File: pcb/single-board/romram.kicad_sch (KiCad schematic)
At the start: 26 parts, among them U10 74HC00, U11 74HC273, U12 74HC273, U13 74HC245, U14 74HC245, U15 SST39SF040, U16 AS6C4008, U17 CY62256, U5 74HC688, U6 74HC688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

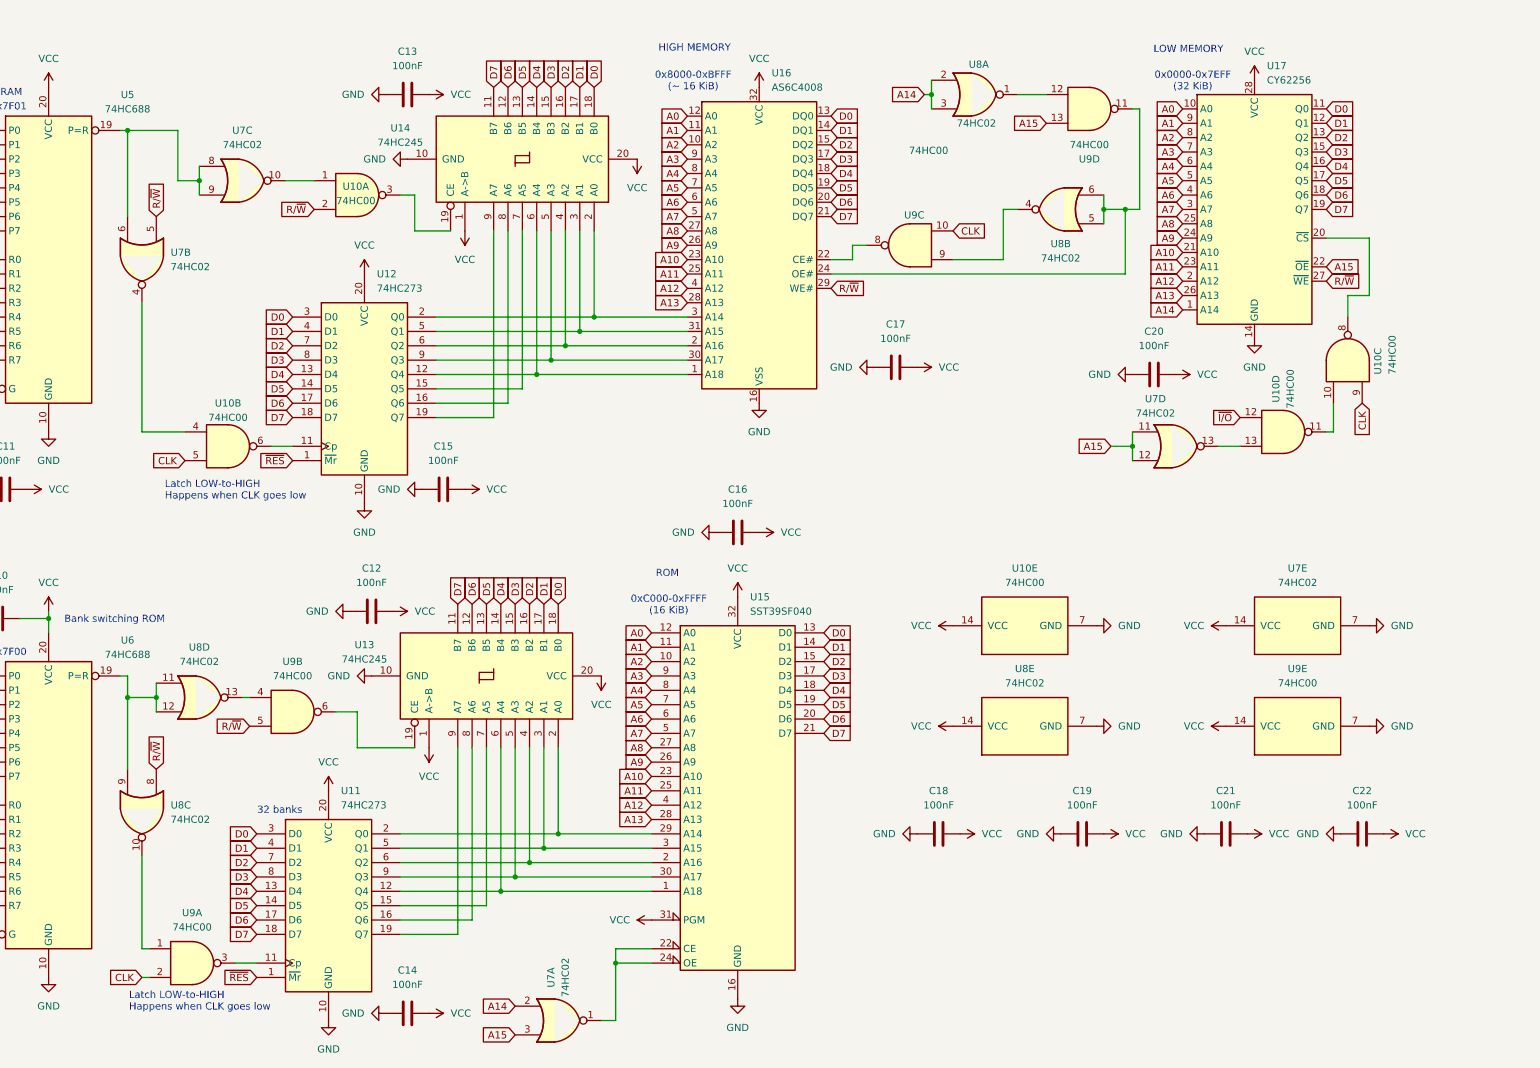
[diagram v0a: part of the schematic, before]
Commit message: Fixing mistake
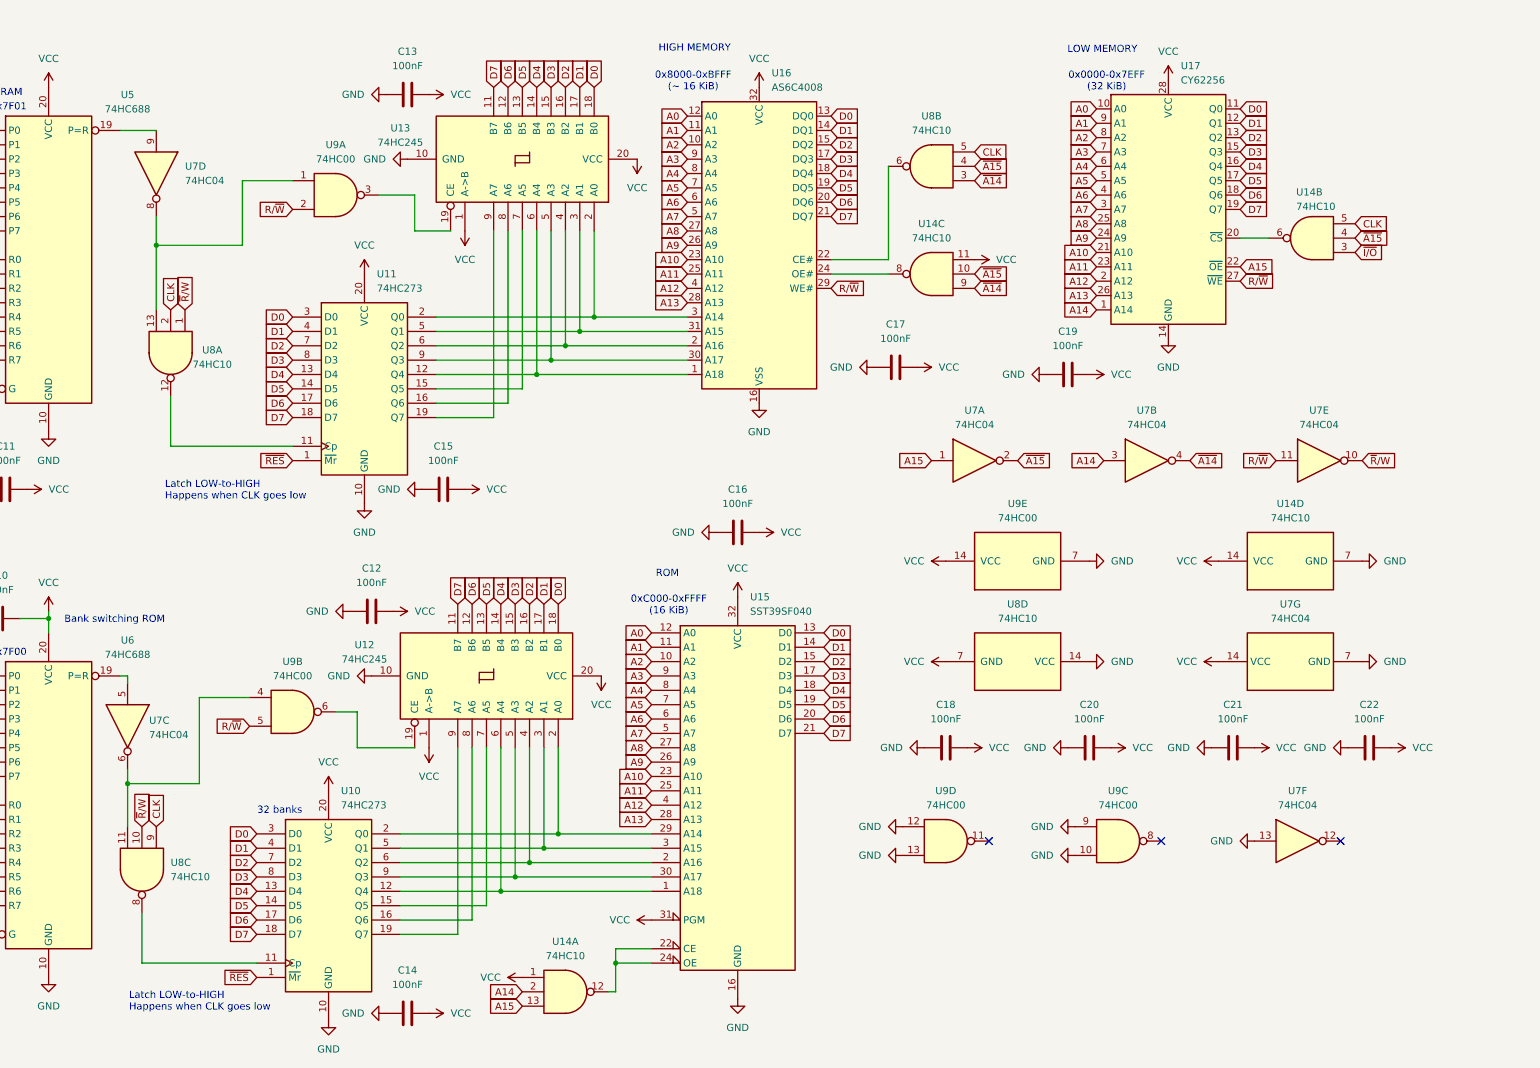
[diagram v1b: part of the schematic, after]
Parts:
- removed U10: 74HC00, Package_DIP:DIP-14_W7.62mm_Socket, symbol 74xx:74HC00
- removed U7, U8: 74HC02, Package_DIP:DIP-14_W7.62mm_Socket, symbol 74xx:74HC02
- added U14, U8: 74HC10, Package_DIP:DIP-14_W7.62mm_Socket, symbol 74xx:74LS10
- added U7: 74HC04, Package_DIP:DIP-14_W7.62mm_Socket, symbol 74xx:74HC04
- renumbered C20 to C19, C19 to C20, U11 to U10, U12 to U11, U13 to U12, U14 to U13
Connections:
- net A14: now also U14.2, U7.3
- net A15: now also U14.13, U7.1; no longer U9.13
- net CLK: now also U14.5, U8.2, U8.5, U8.9; no longer U9.10, U9.2
- net GND: now also U9.10, U9.12, U9.13, U9.9, U14.7 (GND), U7.13, U7.7 (GND), U8.14 (VCC)
- net R/~{W}: now also U9.2, U7.11
- net VCC: now also U14.1, U14.11, U14.14 (VCC), U7.14 (VCC), U8.7 (GND)
- net ~{I/O}: now also U14.3
- net at U15.22 (CE), U15.24 (OE): now also U14.12
- net at U16.24 (OE#): now also U14.8; no longer U9.11
- net at U11.11 (Cp): now also U8.12
- net at U17.20 (~{CS}): now also U14.6
- net at U5.19 (P=R): now also U7.9
- net at U13.19 (CE): now also U9.3
- net at U9.1: now also U7.8, U8.13
- net at U10.11 (Cp): now also U8.8; no longer U9.3
- net at U6.19 (P=R): now also U7.5
- net at U9.4: now also U7.6, U8.11
- net at U9.8: no longer U16.22 (CE#)
- new net: U16.22 (CE#), U8.6
- new net ~{A14}: U14.9, U7.4, U8.3
- new net ~{A15}: U14.10, U14.4, U7.2, U8.4
- new net ~{R}/W: U7.10, U8.1, U8.10
- no-connect marks 0 -> 3
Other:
- moved on the sheet: C18, C19, C20, C21, C22, U17

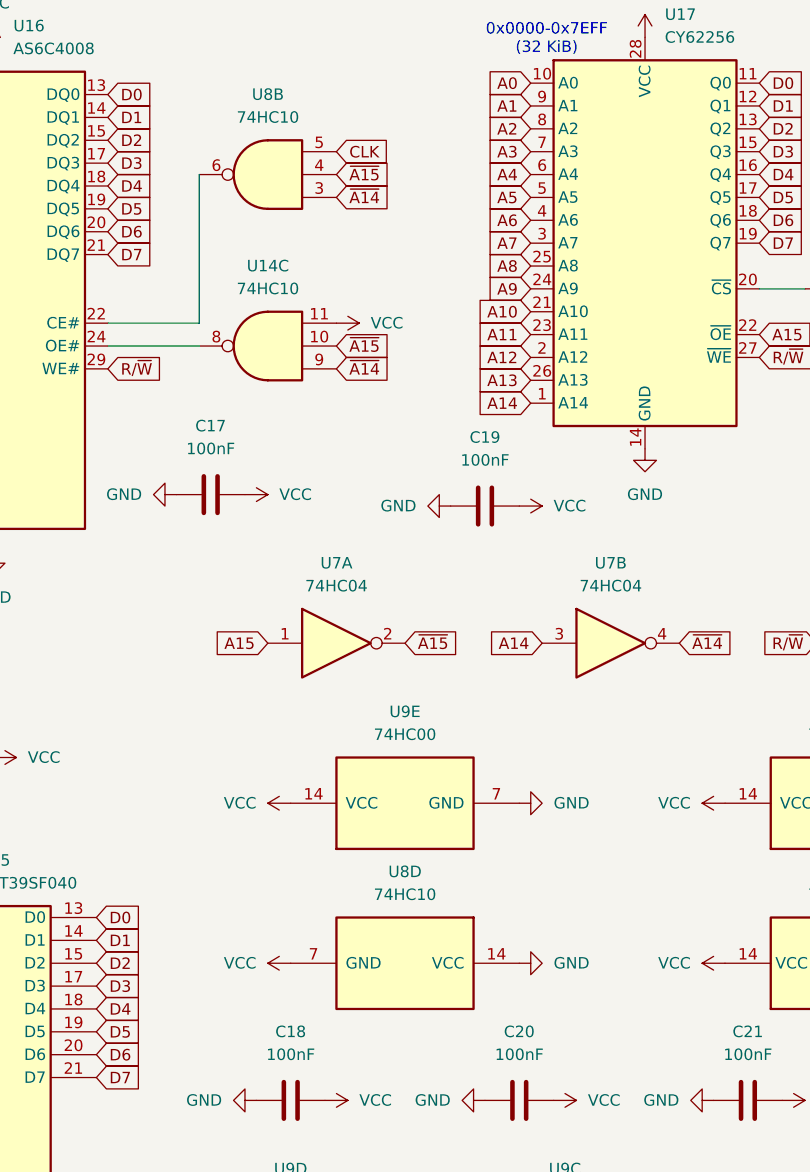
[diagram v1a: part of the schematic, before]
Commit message: Fixing errors and finalizing SBC design
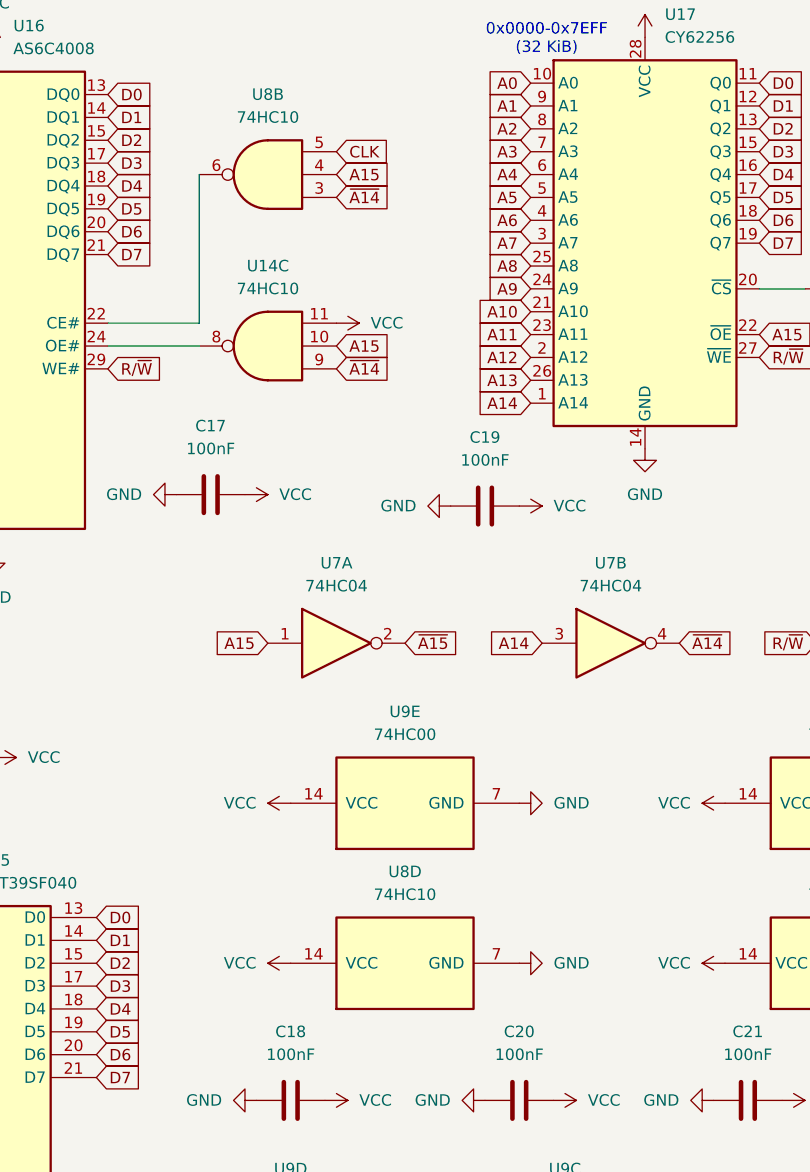
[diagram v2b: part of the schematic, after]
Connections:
- net A15: now also U14.10, U8.4
- net GND: now also U8.7 (GND); no longer U8.14 (VCC)
- net VCC: now also U8.14 (VCC); no longer U8.7 (GND)
- net ~{A15}: no longer U14.10, U8.4
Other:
- moved on the sheet: U8D
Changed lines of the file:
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@@
 		)
 	)
+	(global_label "A15"
+		(shape input)
+		(at 201.93 40.64 0)
+		(fields_autoplaced yes)
+		(effects
+			(font
+				(size 1.27 1.27)
+			)
+			(justify left)
+		)
+		(property "Intersheetrefs" "${INTERSHEET_REFS}"
+			(at 208.4228 40.64 0)
+			(effects
+				(font
+					(size 1.27 1.27)
+				)
+				(justify left)
+				(hide yes)
+			)
+		)
+	)
 	(global_label "A11"
 		(shape input)
@@
 		)
 	)
-	(global_label "~{A15}"
-		(shape input)
-		(at 201.93 40.64 0)
-		(fields_autoplaced yes)
-		(effects
-			(font
-				(size 1.27 1.27)
-			)
-			(justify left)
-		)
-		(property "Intersheetrefs" "${INTERSHEET_REFS}"
-			(at 208.4228 40.64 0)
-			(effects
-				(font
-					(size 1.27 1.27)
-				)
-				(justify left)
-				(hide yes)
-			)
-		)
-	)
 	(global_label "D1"
 		(shape input)
@@
 		)
 	)
-	(global_label "~{A15}"
-		(shape input)
-		(at 201.93 59.69 0)
-		(fields_autoplaced yes)
-		(effects
-			(font
-				(size 1.27 1.27)
-			)
-			(justify left)
-		)
-		(property "Intersheetrefs" "${INTERSHEET_REFS}"
-			(at 208.4228 59.69 0)
-			(effects
-				(font
-					(size 1.27 1.27)
-				)
-				(justify left)
-				(hide yes)
-			)
-		)
-	)
 	(global_label "A4"
 		(shape input)
@@
 		)
 	)
+	(global_label "A15"
+		(shape input)
+		(at 201.93 59.69 0)
+		(fields_autoplaced yes)
+		(effects
+			(font
+				(size 1.27 1.27)
+			)
+			(justify left)
+		)
+		(property "Intersheetrefs" "${INTERSHEET_REFS}"
+			(at 208.4228 59.69 0)
+			(effects
+				(font
+					(size 1.27 1.27)
+				)
+				(justify left)
+				(hide yes)
+			)
+		)
+	)
 	(global_label "D0"
 		(shape input)
@@
 	(symbol
 		(lib_id "74xx:74LS10")
-		(at 209.55 128.27 270)
+		(at 209.55 128.27 90)
 		(unit 4)
 		(exclude_from_sim no)

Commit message: Revising board and adding logo
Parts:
- U16: footprint Package_DIP:DIP-32_W15.24mm -> Package_DIP:DIP-32_W15.24mm_Socket
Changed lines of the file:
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@@
 			)
 		)
-		(property "Footprint" "Package_DIP:DIP-32_W15.24mm"
+		(property "Footprint" "Package_DIP:DIP-32_W15.24mm_Socket"
 			(at 163.83 52.07 0)
 			(effects

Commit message: Further revising
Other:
- note added: "0x0000-0x7EFF (32 KiB) [~{A15} & I/O]"
- note added: "0x8000-0xBFFF (~ 16 KiB) [A15 & ~{A14}]"
- note added: "RAM / ROM"
- note removed: "0x0000-0x7EFF (32 KiB)"
- note removed: "0x8000-0xBFFF (~ 16 KiB)"
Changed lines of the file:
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@@
 		)
 	)
-	(text "0x8000-0xBFFF\n(~ 16 KiB)"
+	(text "0x8000-0xBFFF\n(~ 16 KiB)\n[A15 & ~{A14}]"
 		(exclude_from_sim no)
 		(at 152.146 25.654 0)
@@
 	(text "LOW MEMORY"
 		(exclude_from_sim no)
-		(at 224.536 20.066 0)
+		(at 224.79 18.796 0)
 		(effects
 			(font
@@
 		)
 	)
+	(text "RAM / ROM"
+		(exclude_from_sim no)
+		(at 24.892 16.256 0)
+		(effects
+			(font
+				(size 2.54 2.54)
+				(thickness 0.508)
+				(bold yes)
+			)
+		)
+	)
 	(text "Latch LOW-to-HIGH\nHappens when CLK goes low"
 		(exclude_from_sim no)
@@
 		)
 	)
-	(text "0x0000-0x7EFF\n(32 KiB)"
+	(text "0x0000-0x7EFF\n(32 KiB)\n[~{A15} & I/O]"
 		(exclude_from_sim no)
-		(at 225.298 25.654 0)
+		(at 224.79 24.384 0)
 		(effects
 			(font

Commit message: Refactoring source
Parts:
- U14, U8: value 74HC10 -> 74AC10
- U16: value AS6C4008 -> AS6C4008-55
- U17: value CY62256 -> 62256-55
- U5, U6: value 74HC688 -> CD74HC688
- U7: value 74HC04 -> 74AC04
- U9: value 74HC00 -> 74AC00
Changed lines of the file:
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@@
 			)
 		)
-		(property "Value" "CY62256"
+		(property "Value" "62256-55"
 			(at 238.4141 25.4 0)
 			(effects
@@
 			)
 		)
-		(property "Value" "74HC688"
+		(property "Value" "CD74HC688"
 			(at 52.07 30.5114 0)
 			(effects
@@
 			)
 		)
-		(property "Value" "74HC04"
+		(property "Value" "74AC04"
 			(at 232.41 86.36 0)
 			(effects
@@
 			)
 		)
-		(property "Value" "74HC04"
+		(property "Value" "74AC04"
 			(at 201.93 86.36 0)
 			(effects
@@
 			)
 		)
-		(property "Value" "74HC10"
+		(property "Value" "74AC10"
 			(at 257.81 102.87 90)
 			(effects
@@
 			)
 		)
-		(property "Value" "74HC10"
+		(property "Value" "74AC10"
 			(at 209.55 120.65 90)
 			(effects
@@
 			)
 		)
-		(property "Value" "74HC00"
+		(property "Value" "74AC00"
 			(at 81.2717 130.81 0)
 			(effects
@@
 			)
 		)
-		(property "Value" "74HC04"
+		(property "Value" "74AC04"
 			(at 257.81 120.65 90)
 			(effects
@@
 			)
 		)
-		(property "Value" "74HC10"
+		(property "Value" "74AC10"
 			(at 258.826 47.752 0)
 			(effects
@@
 			)
 		)
-		(property "Value" "74HC00"
+		(property "Value" "74AC00"
 			(at 227.3217 153.67 0)
 			(effects
@@
 			)
 		)
-		(property "Value" "74HC10"
+		(property "Value" "74AC10"
 			(at 67.056 75.692 90)
 			(effects
@@
 			)
 		)
-		(property "Value" "74HC10"
+		(property "Value" "74AC10"
 			(at 194.3183 53.34 0)
 			(effects
@@
 			)
 		)
-		(property "Value" "74HC04"
+		(property "Value" "74AC04"
 			(at 62.23 43.1799 90)
 			(effects
@@
 			)
 		)
-		(property "Value" "74HC04"
+		(property "Value" "74AC04"
 			(at 55.88 141.224 90)
 			(effects
@@
 			)
 		)
-		(property "Value" "74HC10"
+		(property "Value" "74AC10"
 			(at 59.69 166.3616 90)
 			(effects
@@
 			)
 		)
-		(property "Value" "AS6C4008"
+		(property "Value" "AS6C4008-55"
 			(at 166.0241 26.67 0)
 			(effects
@@
 			)
 		)
-		(property "Value" "74HC04"
+		(property "Value" "74AC04"
 			(at 259.08 153.67 0)
 			(effects
@@
 			)
 		)
-		(property "Value" "74HC04"
+		(property "Value" "74AC04"
 			(at 262.89 86.36 0)
 			(effects
@@
 			)
 		)
-		(property "Value" "74HC00"
+		(property "Value" "74AC00"
 			(at 209.55 102.87 90)
 			(effects
@@
 			)
 		)
-		(property "Value" "74HC10"
+		(property "Value" "74AC10"
 			(at 129.5317 180.34 0)
 			(effects
@@
 			)
 		)
-		(property "Value" "74HC00"
+		(property "Value" "74AC00"
 			(at 196.8417 153.67 0)
 			(effects
@@
 			)
 		)
-		(property "Value" "74HC688"
+		(property "Value" "CD74HC688"
 			(at 52.07 127.0314 0)
 			(effects
@@
 			)
 		)
-		(property "Value" "74HC10"
+		(property "Value" "74AC10"
 			(at 194.3183 34.29 0)
 			(effects
@@
 			)
 		)
-		(property "Value" "74HC00"
+		(property "Value" "74AC00"
 			(at 88.8917 39.37 0)
 			(effects

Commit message: Integrating NCURSES into emulator
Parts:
- U15: footprint Socket:DIP_Socket-32_W11.9_W12.7_W15.24_W17.78_W18.5_3M_232-1285-00-0602J -> Package_DIP:DIP-32_W15.24mm_Socket
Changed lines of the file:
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@@
 			)
 		)
-		(property "Footprint" "Socket:DIP_Socket-32_W11.9_W12.7_W15.24_W17.78_W18.5_3M_232-1285-00-0602J"
+		(property "Footprint" "Package_DIP:DIP-32_W15.24mm_Socket"
 			(at 160.02 146.05 0)
 			(effects
